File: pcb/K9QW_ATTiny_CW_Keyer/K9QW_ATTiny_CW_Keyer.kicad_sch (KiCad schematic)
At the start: 33 parts, among them J1 Power Input, J2 AudioJack4, J3 AudioJack4, J4 Sidetone, J5 Mounting Hole, Q1 AO3401A, Q2 MMBT3904, Q3 MMBT2222A, Q4 MMBT3904, SW1 Power Switch, SW2 Command, U1 ATtiny85-20P, U2 LD1117S33TR_SOT223

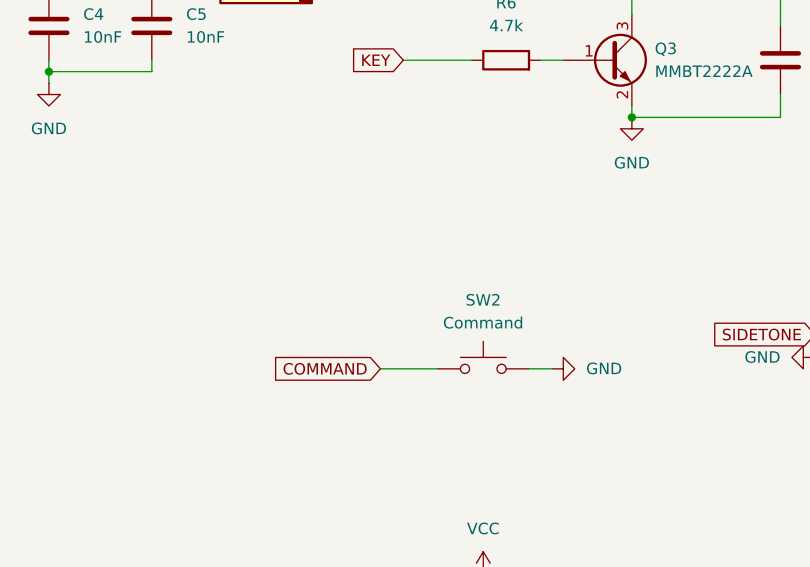
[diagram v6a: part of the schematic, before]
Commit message: Filter cap for command button
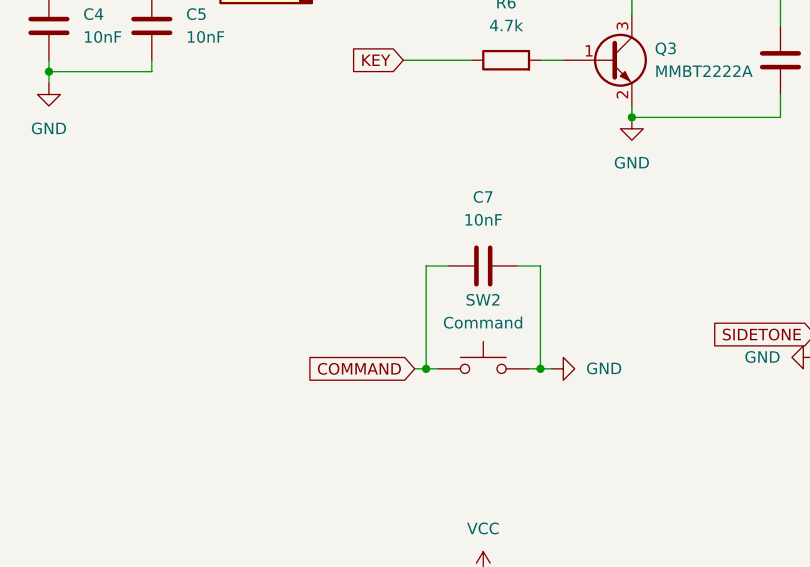
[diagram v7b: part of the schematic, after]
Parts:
- added C7: 10nF, Capacitor_SMD:C_0603_1608Metric_Pad1.08x0.95mm_HandSolder, symbol Device:C
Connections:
- net COMMAND: now also C7.1
- net GND: now also C7.2
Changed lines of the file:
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@@
+	)
+	(junction
+		(at 205.74 88.9)
+		(diameter 0)
+		(color 0 0 0 0)
 	)
 	(junction
@@
 	)
 	(junction
+		(at 193.04 88.9)
+		(diameter 0)
+		(color 0 0 0 0)
+	)
+	(junction
 		(at 63.5 91.44)
 		(diameter 0)
@@
 	(wire
 		(pts
+			(xy 193.04 88.9) (xy 194.31 88.9)
+		)
+		(stroke
+			(width 0)
+			(type default)
+		)
+	)
+	(wire
+		(pts
+			(xy 205.74 88.9) (xy 207.01 88.9)
+		)
+		(stroke
+			(width 0)
+			(type default)
+		)
+	)
+	(wire
+		(pts
 			(xy 52.07 167.64) (xy 90.17 167.64)
 		)
@@
 	(wire
 		(pts
+			(xy 203.2 77.47) (xy 205.74 77.47)
+		)
+		(stroke
+			(width 0)
+			(type default)
+		)
+	)
+	(wire
+		(pts
 			(xy 63.5 91.44) (xy 64.77 91.44)
 		)
@@
 	(wire
 		(pts
+			(xy 193.04 77.47) (xy 193.04 88.9)
+		)
+		(stroke
+			(width 0)
+			(type default)
+		)
+	)
+	(wire
+		(pts
 			(xy 135.89 88.9) (xy 135.89 78.74)
 		)
@@
 	(wire
 		(pts
-			(xy 204.47 88.9) (xy 207.01 88.9)
+			(xy 204.47 88.9) (xy 205.74 88.9)
 		)
 		(stroke
@@
 	(wire
 		(pts
+			(xy 205.74 77.47) (xy 205.74 88.9)
+		)
+		(stroke
+			(width 0)
+			(type default)
+		)
+	)
+	(wire
+		(pts
 			(xy 199.39 111.76) (xy 199.39 114.3)
 		)
@@
 	(wire
 		(pts
+			(xy 195.58 77.47) (xy 193.04 77.47)
+		)
+		(stroke
+			(width 0)
+			(type default)
+		)
+	)
+	(wire
+		(pts
 			(xy 232.41 39.37) (xy 234.95 39.37)
 		)
@@
 	(wire
 		(pts
-			(xy 187.96 88.9) (xy 194.31 88.9)
+			(xy 191.77 88.9) (xy 193.04 88.9)
 		)
 		(stroke
@@
 	(global_label "COMMAND"
 		(shape input)
-		(at 187.96 88.9 180)
+		(at 191.77 88.9 180)
 		(fields_autoplaced yes)
 		(effects
@@
 		)
 		(property "Intersheetrefs" "${INTERSHEET_REFS}"
-			(at 175.7824 88.9 0)
+			(at 179.5924 88.9 0)
 			(effects
 				(font
@@
 					(unit 1)
 				)
+			)
+		)
+	)
+	(symbol
+		(lib_id "Device:C")
+		(at 199.39 77.47 90)
+		(unit 1)
+		(exclude_from_sim no)
+		(in_bom yes)
+		(on_board yes)
+		(dnp no)
+		(fields_autoplaced yes)
+		(property "Reference" "C7"
+			(at 199.39 69.85 90)
+			(effects
+				(font
+					(size 1.27 1.27)
+				)
+			)
+		)
+		(property "Value" "10nF"
+			(at 199.39 72.39 90)
+			(effects
+				(font
+					(size 1.27 1.27)
+				)
+			)
+		)
+		(property "Footprint" "Capacitor_SMD:C_0603_1608Metric_Pad1.08x0.95mm_HandSolder"
+			(at 203.2 76.5048 0)
+			(effects
+				(font
+					(size 1.27 1.27)
+				)
+				(hide yes)
+			)
+		)
+		(property "Datasheet" "~"
+			(at 199.39 77.47 0)
+			(effects
+				(font
+					(size 1.27 1.27)
+				)
+				(hide yes)
+			)
+		)
+		(property "Description" "Unpolarized capacitor"
+			(at 199.39 77.47 0)
+			(effects
+				(font
+					(size 1.27 1.27)
+				)
+				(hide yes)
+			)
+		)
+		(pin "2"
+		)
+		(pin "1"
+		)
+		(instances
+			(project "K9QW_ATTiny_CW_Keyer"
+				(path "/aef77cdf-c6ea-4cd5-9717-5394839cbff2"
+					(reference "C7")
+					(unit 1)
+				)

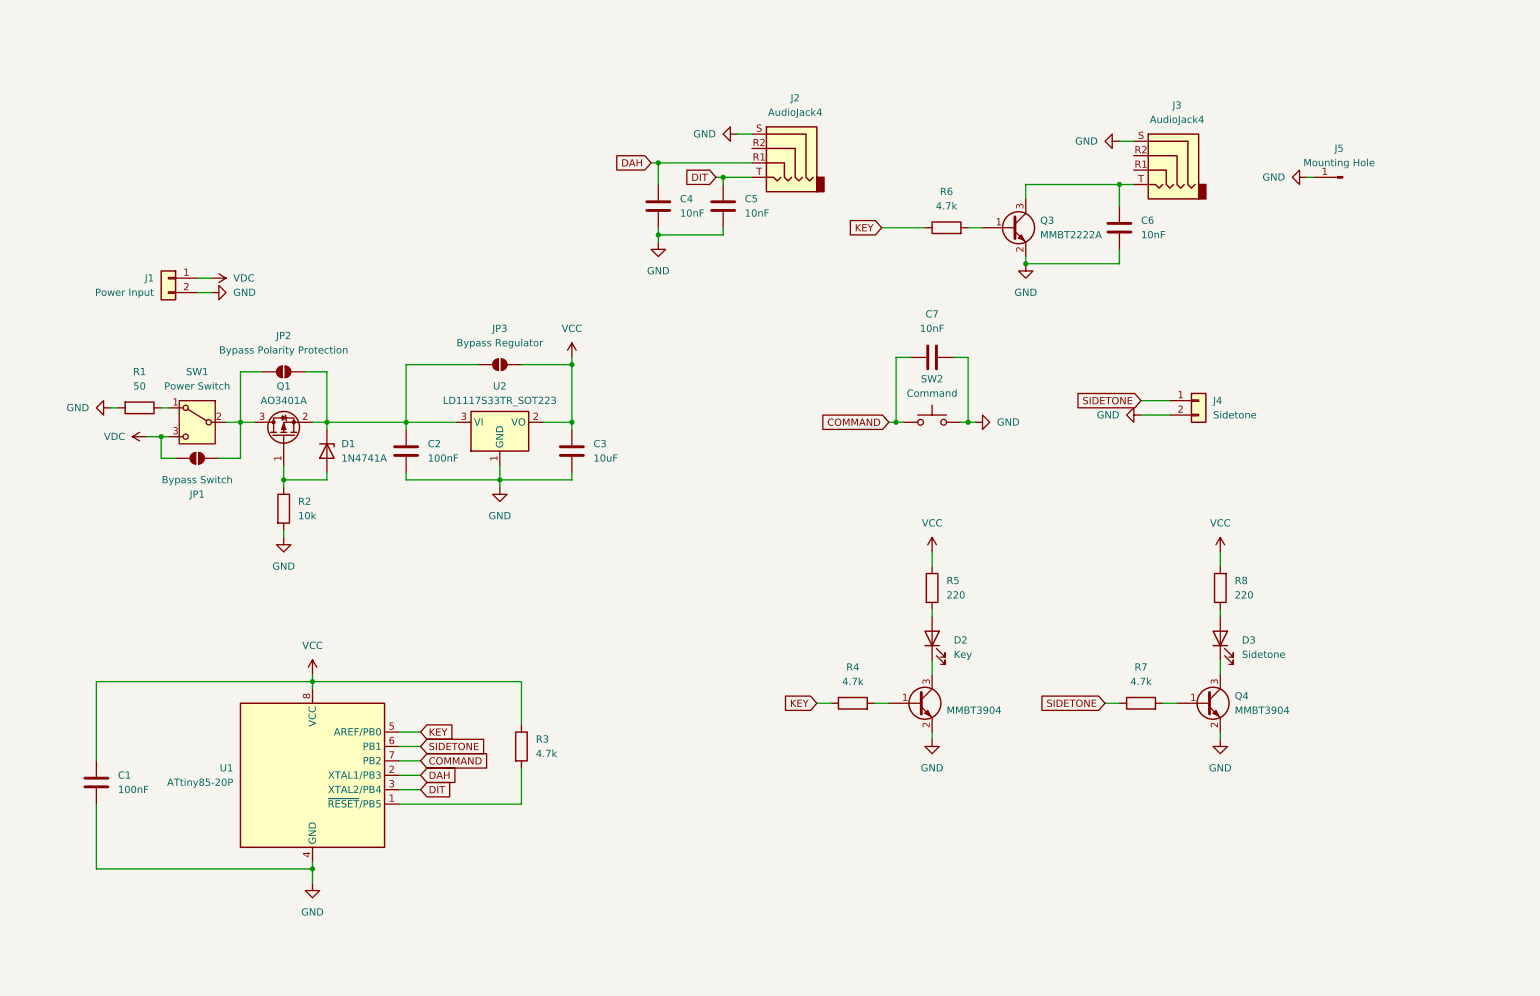
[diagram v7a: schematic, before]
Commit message: Optional LPF and reordering input/output connectors
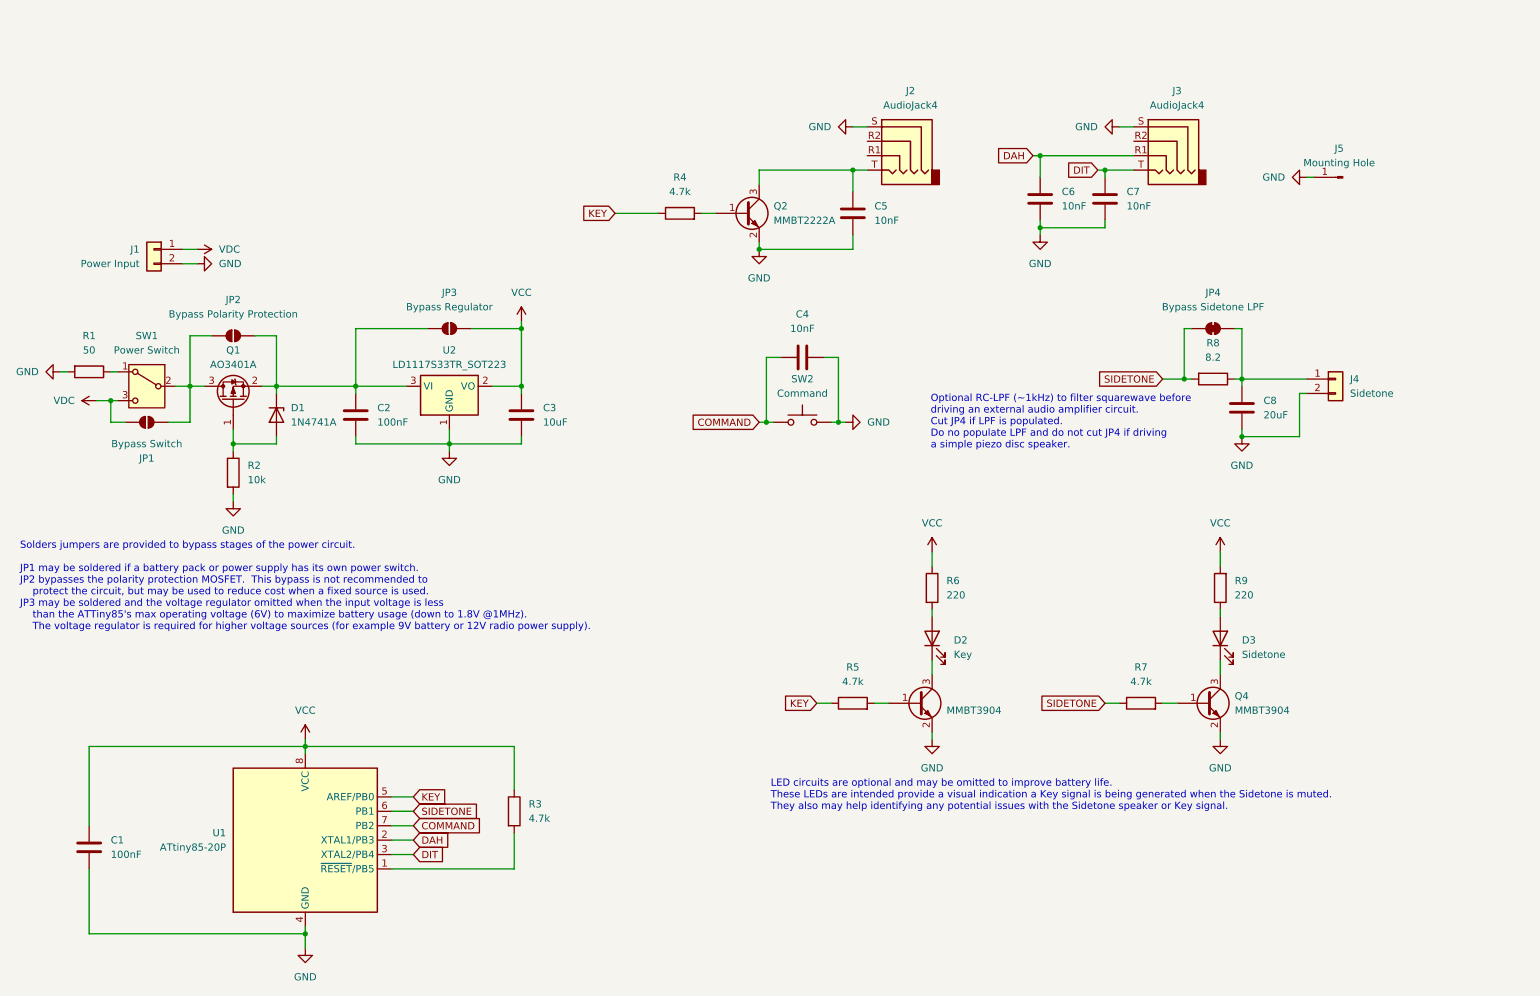
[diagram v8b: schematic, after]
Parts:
- added C8: 20uF, Capacitor_SMD:C_0603_1608Metric_Pad1.08x0.95mm_HandSolder, symbol Device:C
- added JP4: Bypass Sidetone LPF, Jumper:SolderJumper-2_P1.3mm_Bridged_RoundedPad1.0x1.5mm, symbol Jumper:SolderJumper_2_Bridged
- added R8: 8.2, Resistor_SMD:R_0603_1608Metric_Pad0.98x0.95mm_HandSolder, symbol Device:R
- renumbered C7 to C4, C6 to C5, C4 to C6, C5 to C7, J3 to J2, J2 to J3, Q3 to Q2, Q2 to Q3, R6 to R4, R4 to R5, R5 to R6, R8 to R9
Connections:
- net GND: now also C8.2
- net SIDETONE: now also JP4.1 (A), R8.2; no longer J4.1 (Pin_1)
- new net: C8.1, J4.1 (Pin_1), JP4.2 (B), R8.1
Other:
- note added: "LED circuits are optional and may be omitted to improve battery life. These LEDs are intended provide a visual indication a Key signal is being generated when the Sidetone is muted. They also may help identifying any potential issues with the Sidetone speaker or Key signal."
- note added: "Optional RC-LPF (~1kHz) to filter squarewave before driving an external audio amplifier circuit. Cut JP4 if LPF is populated. Do no populate LPF and do not cut JP4 if driving a simple piezo disc speaker."
- note added: "Solders jumpers are provided to bypass stages of the power circuit. JP1 may be soldered if a battery pack or power supply has its own power switch. JP2 bypasses the polarity protection MOSFET. This bypass is not recommended to protect the circuit, but may be used to reduce cost when a fixed source is used. JP3 may be soldered and the voltage regulator omitted when the input voltage is less than t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"
- moved on the sheet: C1, C2, C3, C4, C5, C6, C7, D1, J1, J2, J3, J4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
